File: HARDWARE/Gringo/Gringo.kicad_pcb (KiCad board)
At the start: 2 copper layers, 201 x 48 mm, 64 parts, among them J1 Conn_01x06, J10 Conn_01x06, J11 Conn_01x06, J12 Conn_01x06, J13 Conn_01x06, J14 Conn_01x06, J15 Conn_01x06, J16 Conn_01x06, J17 Conn_01x05_Pin, J2 Conn_01x06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

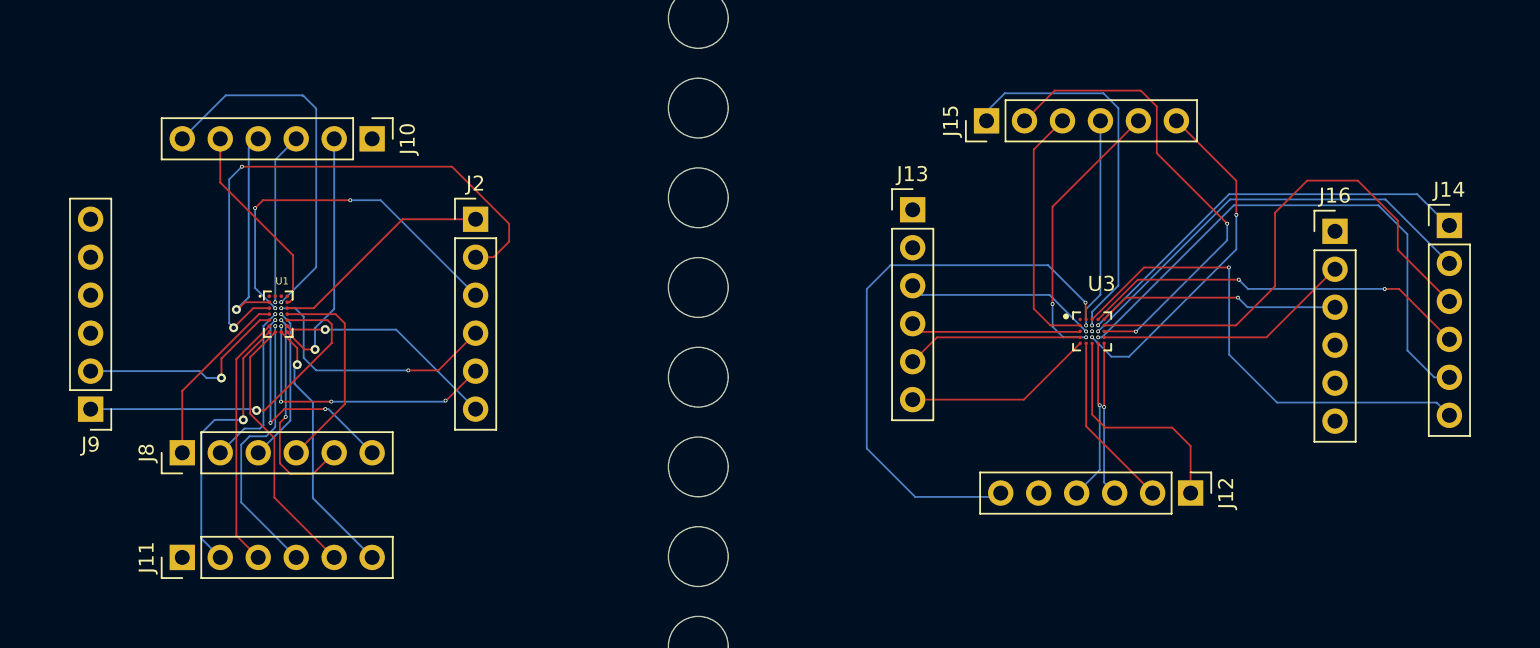
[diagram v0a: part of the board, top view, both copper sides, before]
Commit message: Correction before buy JLCPCB
Remove of via down to 2 tiny component
Change of clearance of the pads to pass routes
To remove clearance : select all the pads > propriétés > Clearance Overrides and DON T PUT 0 (herited) but something like -0.001
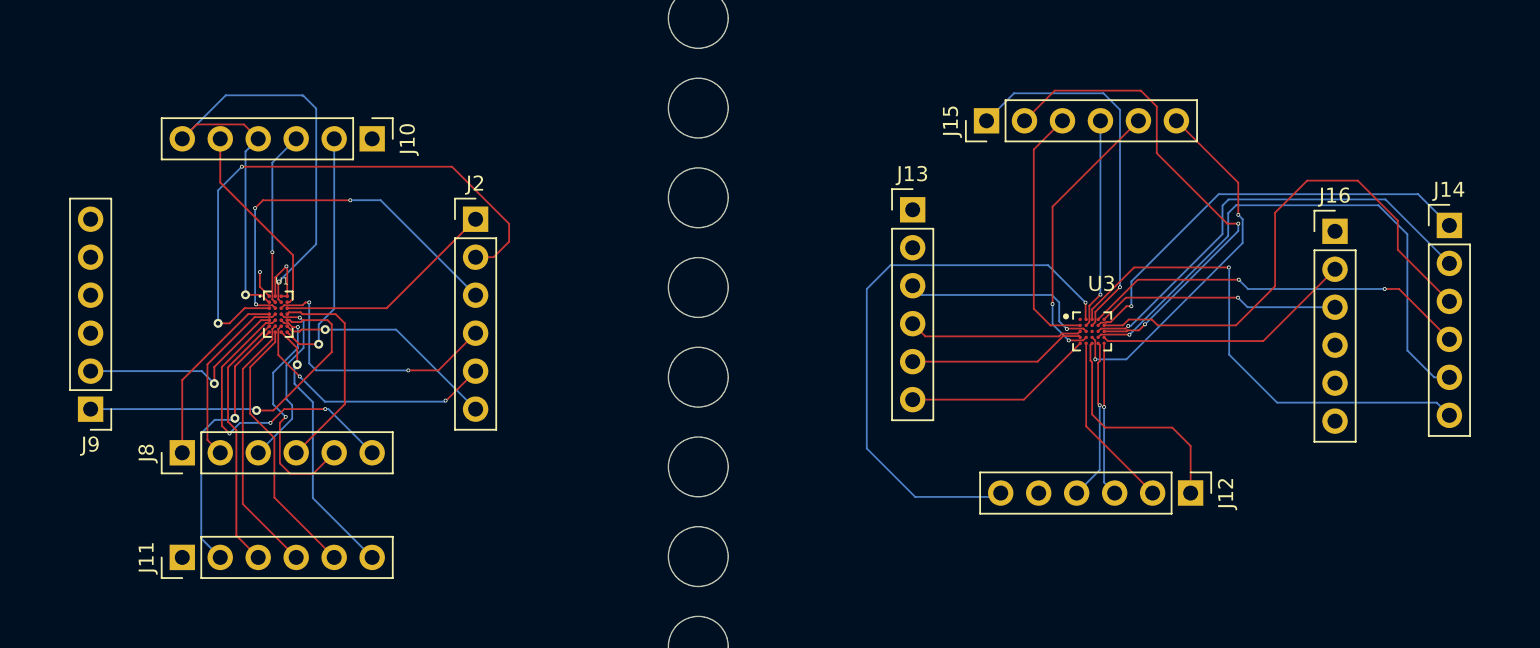
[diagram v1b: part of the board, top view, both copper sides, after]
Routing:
- net GND: track 67.2 -> 73.8 mm, vias 10 -> 12
- net Net-(J8-Pin_6): track 15.4 -> 20.9 mm
- net Net-(J10-Pin_4): track 38.9 -> 43.1 mm
- net Net-(J8-Pin_5): track 14.4 -> 16.1 mm
- net Net-(J8-Pin_3): track 10.4 -> 12.0 mm
- net Net-(J2-Pin_5): track 18.9 -> 17.3 mm, vias 4 -> 2
- net Net-(J15-Pin_6): track 23.4 -> 24.7 mm
- net Net-(J14-Pin_2): track 28.9 -> 30.0 mm
- net Net-(J15-Pin_2): track 31.8 -> 32.9 mm
- net Net-(J2-Pin_4): track 17.4 -> 18.5 mm
- net Net-(J14-Pin_1): track 28.0 -> 29.0 mm
- net Net-(J14-Pin_5): track 36.5 -> 37.4 mm
- net Net-(J2-Pin_2): track 37.5 -> 38.3 mm
- net Net-(J8-Pin_2): track 11.5 -> 12.2 mm, vias 1 -> 0
- net Net-(J13-Pin_3): track 12.9 -> 13.6 mm
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
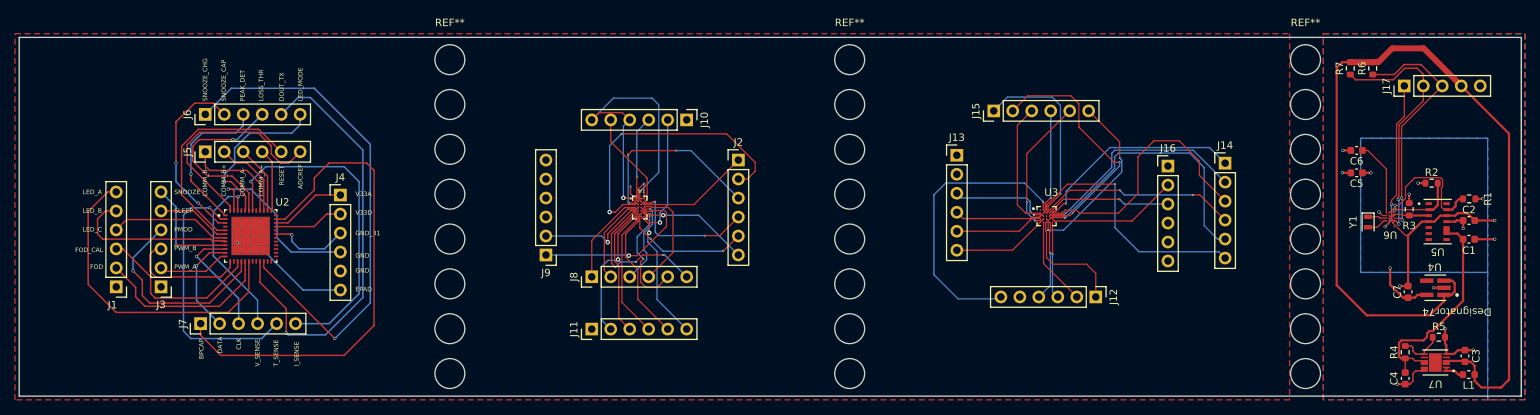
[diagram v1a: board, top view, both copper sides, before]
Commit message: Update scheme and PCB for evk boards with adapted component packages
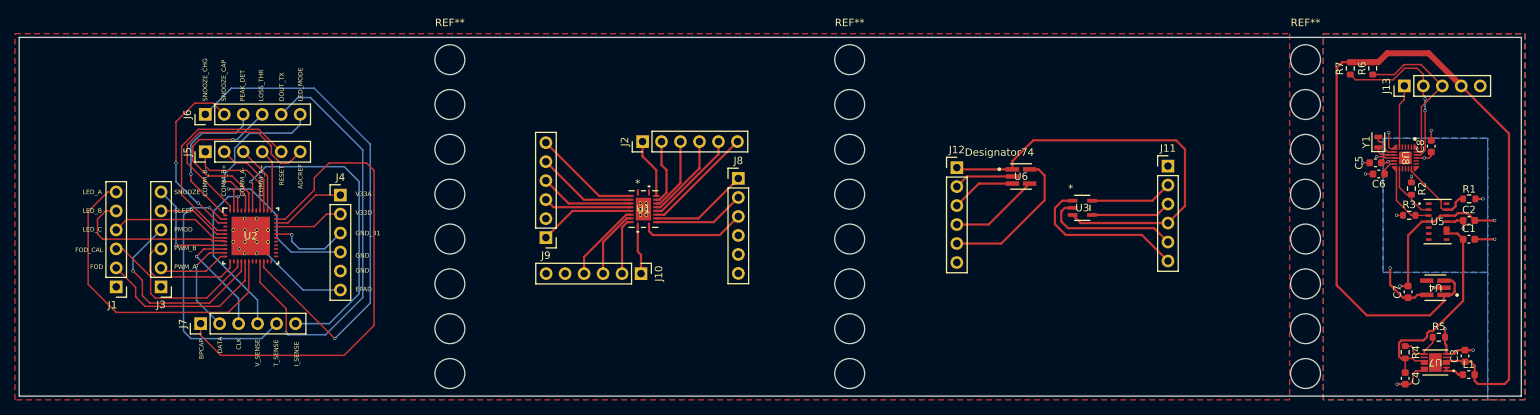
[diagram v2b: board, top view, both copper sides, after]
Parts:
- removed the J12 at (186.1, 100.0)
- removed J14, J15: Conn_01x06, Connector_PinHeader_2.54mm:PinHeader_1x06_P2.54mm_Vertical
- removed J17: Conn_01x05_Pin, Connector_PinHeader_2.54mm:PinHeader_1x05_P2.54mm_Vertical
- removed the J8 at (118.6, 97.3)
- added C8: 1u, Capacitor_SMD:C_0603_1608Metric, F.Cu at (231.0, 79.8)
- added J13: Conn_01x05_Pin, Connector_PinHeader_2.54mm:PinHeader_1x05_P2.54mm_Vertical, F.Cu at (227.4, 71.8)
- added U8: MAX32664GTGA+T, MAX32664GTGA-T:21-100264_T2433&plus_2C_MXM, F.Cu at (227.5, 81.4)
- U1: value BQ51003YFPT -> BQ51013ARHLR; footprint BQ51003YFPT:BGA28N40P7X4_300X188X50N -> BQ51013ARHLR:RHL20_2P05X3P05
- U2: footprint tonpere:IC_BQ500212ARGZT -> BQ500212ARGZT:RGZ0048A
- U3: value BQ25120AYFPT -> MCP73831T-2ACI/OT; footprint BQ25120AYFPT:IC_BQ25120AYFPT -> MCP73831T-2ACI-OT:SOT-23-5_MC_MCH
- U5: footprint MAX30101EFD:21-1048_F143A5&plus_1_MXM-M -> MAX30101EFD-:21-1048_F143A5&plus_1_MXM
- U6: value MAX32664GWEA+T -> PTPS7A2018PDBVR; footprint MAX32664GWEA-T:21-100241A_W161K1&plus_1_MXM -> PTPS7A2018PDBVR:DBV0005A-IPC_A
- moved U6 49.7 mm to (176.1, 83.9), turned to 0 degrees
- moved J8 27.7 mm to (138.2, 84.2), turned to 0 degrees
- moved J9 24.6 mm to (112.5, 92.1), turned to 180 degrees
- moved J2 13.1 mm to (125.4, 79.2), turned to 90 degrees
- moved Y1 10.8 mm to (223.9, 79.3), turned to 90 degrees
- moved J10 9.93 mm to (125.2, 96.9), turned to -90 degrees
- moved U3 4.91 mm to (184.3, 88.1)
- moved C6 4.33 mm to (223.9, 83.5)
- moved C5 2.86 mm to (223.5, 82.0)
- moved R2 2.80 mm to (228.3, 85.5), turned to -90 degrees
- moved J12 1.64 mm to (167.5, 82.7)
- moved R3 0.81 mm to (228.0, 89.1), turned to 0 degrees
- moved U1 0.53 mm to (125.5, 88.2)
- renumbered J11 to J10, J16 to J11, J13 to J12, J9 to J8, J10 to J9
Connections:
- C6 pad 1: Net-(U2-VCORE) -> Net-(U8B-VCORE)
- J10 pad 1: unconnected-(J11-Pin_1-Pad1) -> Net-(J10-Pin_1)
- J10 pad 2: Net-(J11-Pin_2) -> Net-(J10-Pin_2)
- J10 pad 3: Net-(J11-Pin_3) -> Net-(J10-Pin_3)
- J10 pad 4: Net-(J11-Pin_4) -> Net-(J10-Pin_4)
- J10 pad 5: Net-(J11-Pin_5) -> unconnected-(J10-Pin_5-Pad5)
- J10 pad 6: Net-(J11-Pin_6) -> unconnected-(J10-Pin_6-Pad6)
- J11 pad 1: GND -> unconnected-(J11-Pin_1-Pad1)
- J11 pad 2: Net-(J16-Pin_2) -> Net-(J11-Pin_2)
- J11 pad 3: Net-(J16-Pin_3) -> Net-(J11-Pin_3)
- J11 pad 4: unconnected-(J16-Pin_4-Pad4) -> Net-(J11-Pin_4)
- J11 pad 5: unconnected-(J16-Pin_5-Pad5) -> GND
- J11 pad 6: unconnected-(J16-Pin_6-Pad6) -> Net-(J11-Pin_6)
- J12 pad 1: unconnected-(J13-Pin_1-Pad1) -> Net-(J11-Pin_4)
- J12 pad 2: unconnected-(J13-Pin_2-Pad2) -> GND
- J12 pad 3: Net-(J13-Pin_3) -> Net-(J12-Pin_3)
- J12 pad 4: Net-(J13-Pin_4) -> Net-(J12-Pin_4)
- J12 pad 5: Net-(J13-Pin_5) -> Net-(J12-Pin_5)
- J12 pad 6: Net-(J13-Pin_6) -> unconnected-(J12-Pin_6-Pad6)
- J3 pad 2: unconnected-(J3-Pin_2-Pad2) -> Net-(J3-Pin_2)
- J3 pad 3: unconnected-(J3-Pin_3-Pad3) -> Net-(J3-Pin_3)
- J8 pad 1: Net-(J9-Pin_1) -> Net-(J8-Pin_1)
- J8 pad 2: Net-(J9-Pin_2) -> Net-(J8-Pin_2)
- J8 pad 3: GND -> Net-(J8-Pin_3)
- J9 pad 1: unconnected-(J10-Pin_1-Pad1) -> Net-(J9-Pin_1)
- J9 pad 2: Net-(J10-Pin_2) -> unconnected-(J9-Pin_2-Pad2)
- J9 pad 3: Net-(J10-Pin_3) -> Net-(J9-Pin_3)
- J9 pad 4: Net-(J10-Pin_4) -> Net-(J9-Pin_4)
- J9 pad 5: Net-(J10-Pin_5) -> Net-(J9-Pin_5)
- J9 pad 6: Net-(J10-Pin_4) -> Net-(J2-Pin_1)
- U2 pad 12: unconnected-(U2-PWM_A-Pad12) -> Net-(J3-Pin_2)
- U2 pad 13: unconnected-(U2-PWM_B-Pad13) -> Net-(J3-Pin_3)
- Y1 pad 1: Net-(U2-32KIN) -> Net-(U8A-32KIN)
- Y1 pad 2: Net-(U2-32KOUT) -> Net-(U8A-32KOUT)
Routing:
- net Net-(J11-Pin_4): track 17.9 -> 57.4 mm
- net Net-(J12-Pin_6): track 38.6 -> 0.00 mm, vias 1 -> 0
- net Net-(J14-Pin_5): track 37.4 -> 0.00 mm, vias 1 -> 0
- net Net-(J14-Pin_3): track 34.8 -> 0.00 mm
- net Net-(J14-Pin_6): track 33.2 -> 0.00 mm, vias 1 -> 0
- net Net-(J15-Pin_2): track 32.9 -> 0.00 mm, vias 2 -> 0
- net Net-(J10-Pin_4): track 43.1 -> 10.8 mm, vias 2 -> 0
- net Net-(J14-Pin_2): track 30.0 -> 0.00 mm, vias 1 -> 0
- net Net-(J2-Pin_2): track 38.3 -> 8.88 mm, vias 2 -> 0
- net Net-(J14-Pin_1): track 29.0 -> 0.00 mm, vias 1 -> 0
- net (no net): track 26.3 -> 0.00 mm
- net Net-(J14-Pin_4): track 26.2 -> 0.00 mm, vias 2 -> 0
- net Net-(J15-Pin_1): track 25.3 -> 0.00 mm, vias 1 -> 0
- net Net-(J15-Pin_6): track 24.7 -> 0.00 mm, vias 2 -> 0
- net GND: track 73.8 -> 97.3 mm, vias 12 -> 13
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
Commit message: Update inductor package
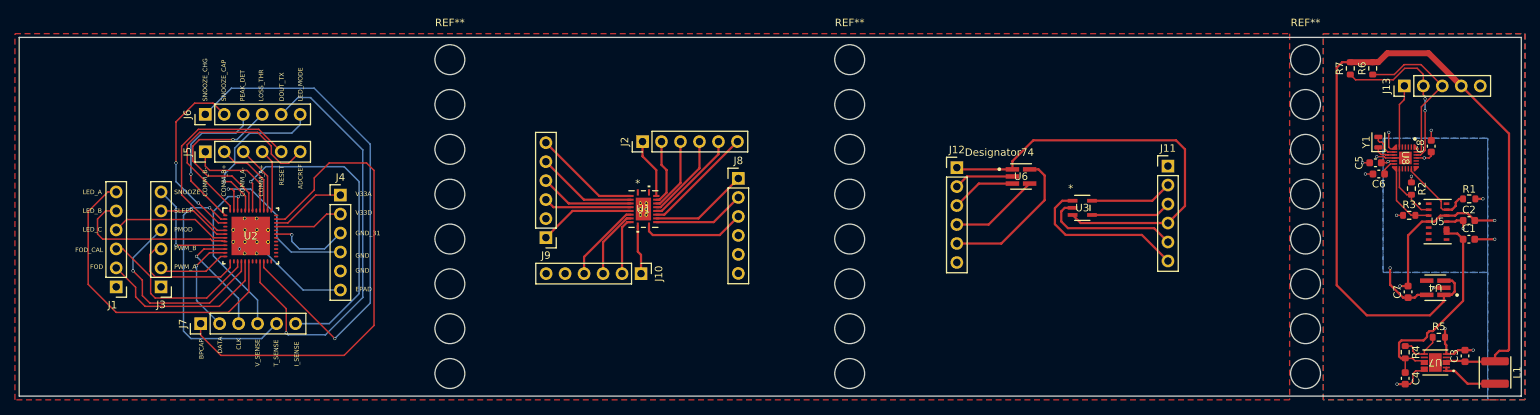
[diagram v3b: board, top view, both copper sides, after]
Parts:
- L1: footprint Inductor_SMD:L_0603_1608Metric -> Inductor_SMD:L_APV_ANR4030
- moved L1 3.53 mm to (239.5, 110.1), turned to -90 degrees
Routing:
- net +3.3V: track 123.4 -> 117.9 mm
- net Net-(L1-Pad2): track 2.85 -> 7.66 mm
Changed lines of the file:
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@@
 		(embedded_fonts no)
 	)
-	(footprint "Inductor_SMD:L_0603_1608Metric"
+	(footprint "Inductor_SMD:L_APV_ANR4030"
 		(layer "F.Cu")
-		(at 235.99 110.395002 180)
-		(descr "Inductor SMD 0603 (1608 Metric), square (rectangular) end terminal, IPC-7351 nominal, (Body size source: http://www.tortai-tech.com/upload/download/2011102023233369053.pdf), generated with kicad-footprint-generator")
-		(tags "inductor")
+		(at 239.51 110.11 -90)
+		(descr "Inductor, APV, ANR4030, 4.0x4.0x3.0mm, (http://en.apvind.com/public/upload/20240407/3375c395e460caa8519b4d637d9113ce.pdf), generated with kicad-footprint-generator gen_inductor.py")
+		(tags "wirewound power shielded")
 		(property "Reference" "L1"
-			(at 0 1.364998 0)
+			(at 0 -2.95 90)
 			(layer "F.SilkS")
 			(effects
@@
 		)
 		(property "Value" "2u2"
-			(at 0 1.43 0)
+			(at 0 2.95 90)
 			(layer "F.Fab")
 			(effects
@@
 		)
 		(property "Datasheet" "~"
-			(at 0 0 0)
+			(at 0 0 90)
 			(layer "F.Fab")
 			(hide yes)
@@
 		)
 		(property "Description" "Inductor"
-			(at 0 0 0)
+			(at 0 0 90)
 			(layer "F.Fab")
 			(hide yes)
@@
 		(attr smd)
 		(fp_line
-			(start -0.162779 0.51)
-			(end 0.162779 0.51)
+			(start 2.11 2.11)
+			(end -2.11 2.11)
 			(stroke
 				(width 0.12)
@@
 		)
 		(fp_line
-			(start -0.162779 -0.51)
-			(end 0.162779 -0.51)
+			(start -2.11 -2.11)
+			(end 2.11 -2.11)
 			(stroke
 				(width 0.12)
@@
 		)
 		(fp_line
-			(start 1.48 0.73)
-			(end -1.48 0.73)
+			(start -2.25 2.25)
+			(end -2.25 2.1)
 			(stroke
 				(width 0.05)
@@
 		)
 		(fp_line
-			(start 1.48 -0.73)
-			(end 1.48 0.73)
+			(start 2.25 2.25)
+			(end -2.25 2.25)
 			(stroke
 				(width 0.05)
@@
 		)
 		(fp_line
-			(start -1.48 0.73)
-			(end -1.48 -0.73)
+			(start -2.3 2.1)
+			(end -2.3 -2.1)
 			(stroke
 				(width 0.05)
@@
 		)
 		(fp_line
-			(start -1.48 -0.73)
-			(end 1.48 -0.73)
+			(start -2.25 2.1)
+			(end -2.3 2.1)
 			(stroke
 				(width 0.05)
@@
 		)
 		(fp_line
-			(start 0.8 0.4)
-			(end -0.8 0.4)
+			(start 2.25 2.1)
+			(end 2.25 2.25)
 			(stroke
-				(width 0.1)
+				(width 0.05)
 				(type solid)
 			)
-			(layer "F.Fab")
+			(layer "F.CrtYd")
 		)
 		(fp_line
-			(start 0.8 -0.4)
-			(end 0.8 0.4)
+			(start 2.3 2.1)
+			(end 2.25 2.1)
 			(stroke
-				(width 0.1)
+				(width 0.05)
 				(type solid)
 			)
-			(layer "F.Fab")
+			(layer "F.CrtYd")
 		)
 		(fp_line
-			(start -0.8 0.4)
-			(end -0.8 -0.4)
+			(start -2.3 -2.1)
+			(end -2.25 -2.1)
 			(stroke
-				(width 0.1)
+				(width 0.05)
 				(type solid)
 			)
-			(layer "F.Fab")
+			(layer "F.CrtYd")
 		)
 		(fp_line
-			(start -0.8 -0.4)
-			(end 0.8 -0.4)
+			(start -2.25 -2.1)
+			(end -2.25 -2.25)
+			(stroke
+				(width 0.05)
+				(type solid)
+			)
+			(layer "F.CrtYd")
+		)
+		(fp_line
+			(start 2.25 -2.1)
+			(end 2.3 -2.1)
+			(stroke
+				(width 0.05)
+				(type solid)
+			)
+			(layer "F.CrtYd")
+		)
+		(fp_line
+			(start 2.3 -2.1)
+			(end 2.3 2.1)
+			(stroke
+				(width 0.05)
+				(type solid)
+			)
+			(layer "F.CrtYd")
+		)
+		(fp_line
+			(start -2.25 -2.25)
+			(end 2.25 -2.25)
+			(stroke
+				(width 0.05)
+				(type solid)
+			)
+			(layer "F.CrtYd")
+		)
+		(fp_line
+			(start 2.25 -2.25)
+			(end 2.25 -2.1)
+			(stroke
+				(width 0.05)
+				(type solid)
+			)
+			(layer "F.CrtYd")
+		)
+		(fp_rect
+			(start -2 -2)
+			(end 2 2)
 			(stroke
 				(width 0.1)
 				(type solid)
 			)
+			(fill no)
 			(layer "F.Fab")
 		)
 		(fp_text user "${REFERENCE}"
-			(at 0 0 0)
+			(at 0 0 90)
 			(layer "F.Fab")
 			(effects
 				(font
-					(size 0.4 0.4)
-					(thickness 0.06)
+					(size 1 1)
+					(thickness 0.15)
 				)
 			)
 		)
 		(pad "1" smd roundrect
-			(at -0.7875 0 180)
-			(size 0.875 0.95)
+			(at -1.5 0 270)
+			(size 1.1 3.7)
 			(layers "F.Cu" "F.Mask" "F.Paste")
-			(roundrect_rratio 0.25)
+			(roundrect_rratio 0.227273)
 			(net 75 "+3.3V")
 			(pinfunction "1")
@@
 		)
 		(pad "2" smd roundrect
-			(at 0.7875 0 180)
-			(size 0.875 0.95)
+			(at 1.5 0 270)
+			(size 1.1 3.7)
 			(layers "F.Cu" "F.Mask" "F.Paste")
-			(roundrect_rratio 0.25)
+			(roundrect_rratio 0.227273)
 			(net 76 "Net-(L1-Pad2)")
 			(pinfunction "2")
@@
 		)
 		(embedded_fonts no)
-		(model "${KICAD9_3DMODEL_DIR}/Inductor_SMD.3dshapes/L_0603_1608Metric.step"
+		(model "${KICAD9_3DMODEL_DIR}/Inductor_SMD.3dshapes/L_APV_ANR4030.step"
 			(offset
 				(xyz 0 0 0)
@@
 		(fp_text user "*"
 			(at -0.75 -3.437401 0)
+			(unlocked yes)
 			(layer "F.SilkS")
 			(effects
@@
 		(fp_text user "*"
 			(at -0.75 -3.437401 0)
-			(unlocked yes)
 			(layer "F.SilkS")
 			(effects
@@
 			(at -0.3937 -0.7874)
 			(size 0.508 0.508)
-			(drill 0.3)
+			(drill 0.254)
 			(layers "*.Cu" "*.Mask")
 			(remove_unused_layers no)
@@
 			(at -0.3937 0)
 			(size 0.508 0.508)
-			(drill 0.3)
+			(drill 0.254)
 			(layers "*.Cu" "*.Mask")
 			(remove_unused_layers no)
@@
 			(at -0.3937 0.7874)
 			(size 0.508 0.508)
-			(drill 0.3)
+			(drill 0.254)
 			(layers "*.Cu" "*.Mask")
 			(remove_unused_layers no)
@@
 			(at 0.3937 -0.7874)
 			(size 0.508 0.508)
-			(drill 0.3)
+			(drill 0.254)
 			(layers "*.Cu" "*.Mask")
 			(remove_unused_layers no)
@@
 			(at 0.3937 0)
 			(size 0.508 0.508)
-			(drill 0.3)
+			(drill 0.254)
 			(layers "*.Cu" "*.Mask")
 			(remove_unused_layers no)
@@
 			(at 0.3937 0.7874)
 			(size 0.508 0.508)
-			(drill 0.3)
+			(drill 0.254)
 			(layers "*.Cu" "*.Mask")
 			(remove_unused_layers no)
@@
 		(fp_text user "*"
 			(at -0.6477 -1.6358 0)
-			(unlocked yes)
 			(layer "F.Fab")
 			(effects
@@
 		(fp_text user "*"
 			(at -0.6477 -1.6358 0)
+			(unlocked yes)
 			(layer "F.Fab")
 			(effects
@@
 	)
 	(segment
-		(start 232.670483 100.589517)
-		(end 230.8 102.46)
+		(start 239.51 107.78)
+		(end 240.08 107.21)
 		(width 0.3)
 		(layer "F.Cu")
@@
 	)
 	(segment
-		(start 219.06 68.59)
-		(end 220.14 68.59)
+		(start 239.51 108.61)
+		(end 239.51 107.78)
 		(width 0.3)
 		(layer "F.Cu")
@@
 	)
 	(segment
-		(start 236.7775 110.395002)
-		(end 236.7775 109.2075)
+		(start 232.670483 100.589517)
+		(end 230.8 102.46)
+		(width 0.3)
+		(layer "F.Cu")
+		(net 75)
+	)
+	(segment
+		(start 219.06 68.59)
+		(end 220.14 68.59)
 		(width 0.3)
 		(layer "F.Cu")
@@
 	)
 	(segment
-		(start 241.38 111.06)
-		(end 241.38 78.15)
+		(start 241.22 107.21)
+		(end 241.38 107.05)
 		(width 0.3)
 		(layer "F.Cu")
@@
 	)
 	(segment
-		(start 236.7775 110.395002)
-		(end 236.7775 111.2275)
+		(start 241.38 107.05)
+		(end 241.38 78.15)
 		(width 0.3)
 		(layer "F.Cu")
@@
 	)
 	(segment
-		(start 240.79 111.65)
-		(end 241.38 111.06)
+		(start 241.38 78.15)
+		(end 234.99 71.76)
 		(width 0.3)
 		(layer "F.Cu")
@@
 	)
 	(segment
-		(start 241.38 78.15)
-		(end 234.99 71.76)
-		(width 0.3)
-		(layer "F.Cu")
-		(net 75)
-	)
-	(segment
 		(start 234.11 99.3)
 		(end 233.689999 99.720001)
@@
 	)
 	(segment
-		(start 236.240002 108.670002)
-		(end 235.49 108.670002)
-		(width 0.3)
-		(layer "F.Cu")
-		(net 75)
-	)
-	(segment
 		(start 218.32 69.33)
 		(end 219.06 68.59)
@@
 	)
 	(segment
-		(start 233.759999 97.819999)
-		(end 234.11 98.17)
+		(start 240.08 107.21)
+		(end 241.22 107.21)
 		(width 0.3)
 		(layer "F.Cu")
@@
 	)
 	(segment
-		(start 236.7775 109.2075)
-		(end 236.240002 108.670002)
+		(start 235.49 108.670002)
+		(end 239.449998 108.670002)
 		(width 0.3)
 		(layer "F.Cu")
@@
 	)
 	(segment
-		(start 237.2 111.65)
-		(end 240.79 111.65)
+		(start 233.759999 97.819999)
+		(end 234.11 98.17)
 		(width 0.3)
 		(layer "F.Cu")
@@
 	)
 	(segment
-		(start 235.49 108.670002)
-		(end 235.380698 108.5607)
+		(start 239.449998 108.670002)
+		(end 239.51 108.61)
 		(width 0.3)
 		(layer "F.Cu")
@@
 	)
 	(segment
-		(start 232.670483 99.720001)
-		(end 232.670483 100.589517)
+		(start 235.49 108.670002)
+		(end 235.380698 108.5607)
 		(width 0.3)
 		(layer "F.Cu")
@@
 	)
 	(segment
-		(start 236.7775 111.2275)
-		(end 237.2 111.65)
+		(start 232.670483 99.720001)
+		(end 232.670483 100.589517)
 		(width 0.3)
 		(layer "F.Cu")
@@
 	)
 	(segment
-		(start 234.615002 110.395002)
-		(end 234.115002 109.895002)
+		(start 234.115002 109.895002)
+		(end 235.83 111.61)
 		(width 0.3)
 		(layer "F.Cu")
@@
 	)
 	(segment
-		(start 232.99 109.895002)
-		(end 232.99 109.460701)
+		(start 235.83 111.61)
+		(end 239.51 111.61)
 		(width 0.3)
 		(layer "F.Cu")
@@
 	)
 	(segment
-		(start 234.115002 109.895002)
-		(end 232.99 109.895002)
+		(start 232.99 109.895002)
+		(end 232.99 109.460701)
 		(width 0.3)
 		(layer "F.Cu")
@@
 	)
 	(segment
-		(start 235.2025 110.395002)
-		(end 234.615002 110.395002)
+		(start 232.99 109.895002)
+		(end 234.115002 109.895002)
 		(width 0.3)
 		(layer "F.Cu")
